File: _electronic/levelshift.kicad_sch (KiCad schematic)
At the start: 10 parts

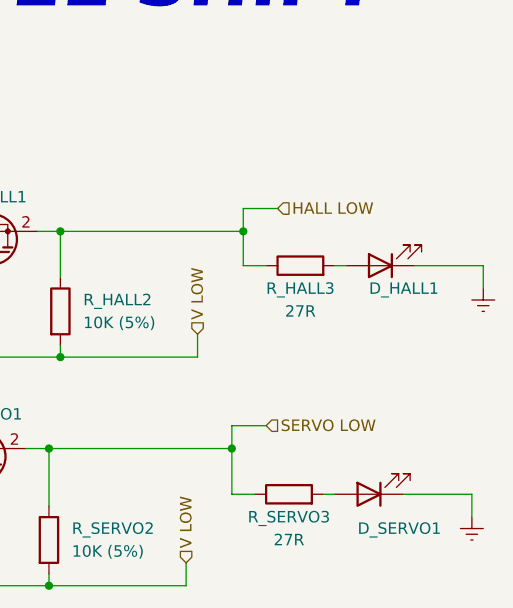
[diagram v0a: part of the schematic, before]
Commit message: revised pcb: direct power, leds, ftdi w/o 3v3
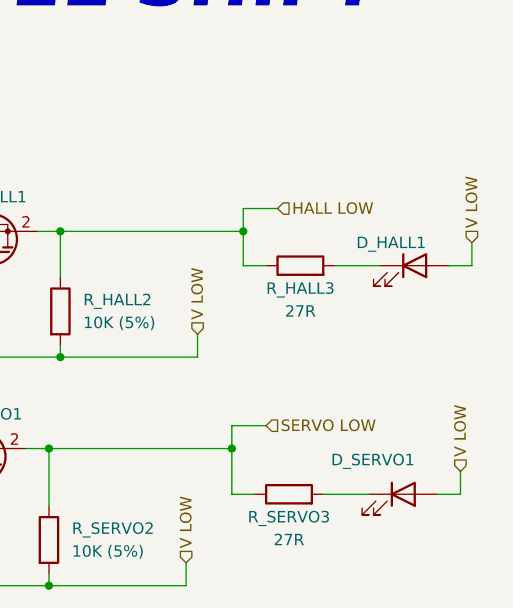
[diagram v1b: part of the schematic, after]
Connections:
- net V LOW: now also D_HALL1.2 (A), D_SERVO1.2 (A)
- net at R_HALL3.2: now also D_HALL1.1 (K); no longer D_HALL1.2 (A)
- net at R_SERVO3.2: now also D_SERVO1.1 (K); no longer D_SERVO1.2 (A)
- removed net GNDREF: D_HALL1.1 (K), D_SERVO1.1 (K)
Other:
- moved on the sheet: D_HALL1, D_SERVO1
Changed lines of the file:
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@@
     (stroke (width 0) (type default) (color 0 0 0 0))
   )
-  (wire (pts (xy 176.53 96.52) (xy 177.8 96.52))
+  (wire (pts (xy 176.53 96.52) (xy 181.61 96.52))
     (stroke (width 0) (type default) (color 0 0 0 0))
   )
@@
     (stroke (width 0) (type default) (color 0 0 0 0))
   )
+  (wire (pts (xy 191.77 93.98) (xy 191.77 96.52))
+    (stroke (width 0) (type default) (color 0 0 0 0))
+  )
   (wire (pts (xy 144.78 132.08) (xy 144.78 130.81))
     (stroke (width 0) (type default) (color 0 0 0 0))
@@
     (stroke (width 0) (type default) (color 0 0 0 0))
   )
-  (wire (pts (xy 176.53 121.92) (xy 175.26 121.92))
+  (wire (pts (xy 180.34 121.92) (xy 175.26 121.92))
     (stroke (width 0) (type default) (color 0 0 0 0))
   )
@@
     (stroke (width 0) (type default) (color 0 0 0 0))
   )
+  (wire (pts (xy 190.5 119.38) (xy 190.5 121.92))
+    (stroke (width 0) (type default) (color 0 0 0 0))
+  )
   (wire (pts (xy 160.02 129.54) (xy 160.02 132.08))
     (stroke (width 0) (type default) (color 0 0 0 0))
@@
     (stroke (width 0) (type default) (color 0 0 0 0))
   )
-  (wire (pts (xy 184.15 121.92) (xy 191.77 121.92))
+  (wire (pts (xy 187.96 121.92) (xy 190.5 121.92))
     (stroke (width 0) (type default) (color 0 0 0 0))
   )
@@
     (stroke (width 0) (type default) (color 0 0 0 0))
   )
-  (wire (pts (xy 191.77 121.92) (xy 191.77 124.46))
-    (stroke (width 0) (type default) (color 0 0 0 0))
-  )
   (wire (pts (xy 161.29 106.68) (xy 161.29 104.14))
     (stroke (width 0) (type default) (color 0 0 0 0))
   )
-  (wire (pts (xy 193.04 96.52) (xy 193.04 99.06))
-    (stroke (width 0) (type default) (color 0 0 0 0))
-  )
-  (wire (pts (xy 185.42 96.52) (xy 193.04 96.52))
+  (wire (pts (xy 189.23 96.52) (xy 191.77 96.52))
     (stroke (width 0) (type default) (color 0 0 0 0))
   )
@@
     (effects (font (size 1.27 1.27)) (justify left))
   )
+  (hierarchical_label "V LOW" (shape input) (at 191.77 93.98 90)
+    (effects (font (size 1.27 1.27)) (justify left))
+  )
   (hierarchical_label "SERVO HIGH" (shape input) (at 115.57 116.84 180)
     (effects (font (size 1.27 1.27)) (justify right))
+  )
+  (hierarchical_label "V LOW" (shape input) (at 190.5 119.38 90)
+    (effects (font (size 1.27 1.27)) (justify left))
   )
   (hierarchical_label "V HIGH" (shape input) (at 118.11 104.14 90)
@@
     (pin "2")
   )
-  (symbol (lib_id "Device:LED") (at 181.61 96.52 180) (unit 1)
-    (in_bom yes) (on_board yes)
-    (property "Reference" "D_HALL1" (id 0) (at 180.34 99.06 0)
+  (symbol (lib_id "Device:LED") (at 185.42 96.52 0) (unit 1)
+    (in_bom yes) (on_board yes)
+    (property "Reference" "D_HALL1" (id 0) (at 186.69 93.98 0)
       (effects (font (size 1.27 1.27)) (justify right))
     )
-    (property "Value" "LED white" (id 1) (at 184.15 91.44 0)
+    (property "Value" "LED white" (id 1) (at 182.88 101.6 0)
       (effects (font (size 1.27 1.27)) (justify left) hide)
     )
-    (property "Footprint" "LED_SMD:LED_0603_1608Metric_Pad1.05x0.95mm_HandSolder" (id 2) (at 181.61 96.52 0)
-      (effects (font (size 1.27 1.27)) hide)
-    )
-    (property "Datasheet" "https://br.mouser.com/datasheet/2/348/smld12-e-1874545.pdf" (id 3) (at 181.61 96.52 0)
-      (effects (font (size 1.27 1.27)) hide)
-    )
-    (property "#" "SMLD12WBN1W1" (id 4) (at 184.15 92.71 90)
+    (property "Footprint" "LED_SMD:LED_0603_1608Metric_Pad1.05x0.95mm_HandSolder" (id 2) (at 185.42 96.52 0)
+      (effects (font (size 1.27 1.27)) hide)
+    )
+    (property "Datasheet" "https://br.mouser.com/datasheet/2/348/smld12-e-1874545.pdf" (id 3) (at 185.42 96.52 0)
+      (effects (font (size 1.27 1.27)) hide)
+    )
+    (property "#" "SMLD12WBN1W1" (id 4) (at 182.88 100.33 90)
       (effects (font (size 1.27 1.27) italic) (justify right) hide)
     )
-    (property "Description" "Signal LED" (id 5) (at 181.61 96.52 0)
-      (effects (font (size 1.27 1.27)) hide)
-    )
-    (property "Group" "Hall" (id 6) (at 181.61 96.52 0)
-      (effects (font (size 1.27 1.27)) hide)
-    )
-    (property "Mouser" "OK" (id 7) (at 181.61 96.52 0)
+    (property "Description" "Signal LED" (id 5) (at 185.42 96.52 0)
+      (effects (font (size 1.27 1.27)) hide)
+    )
+    (property "Group" "Hall" (id 6) (at 185.42 96.52 0)
+      (effects (font (size 1.27 1.27)) hide)
+    )
+    (property "Mouser" "OK" (id 7) (at 185.42 96.52 0)
       (effects (font (size 1.27 1.27)) hide)
     )
@@
     (pin "2")
   )
-  (symbol (lib_id "power:GNDREF") (at 193.04 99.06 0) (unit 1)
-    (in_bom yes) (on_board yes) (fields_autoplaced)
-    (property "Reference" "#PWR0192" (id 0) (at 193.04 105.41 0)
-      (effects (font (size 1.27 1.27)) hide)
-    )
-    (property "Value" "GNDREF" (id 1) (at 193.04 104.14 0)
-      (effects (font (size 1.27 1.27)) hide)
-    )
-    (property "Footprint" "" (id 2) (at 193.04 99.06 0)
-      (effects (font (size 1.27 1.27)) hide)
-    )
-    (property "Datasheet" "" (id 3) (at 193.04 99.06 0)
-      (effects (font (size 1.27 1.27)) hide)
-    )
-    (pin "1")
-  )
   (symbol (lib_id "Transistor_FET:BSS138") (at 138.43 95.25 90) (unit 1)
     (in_bom yes) (on_board yes)
@@
     (pin "3")
   )
-  (symbol (lib_id "Device:LED") (at 180.34 121.92 180) (unit 1)
-    (in_bom yes) (on_board yes)
-    (property "Reference" "D_SERVO1" (id 0) (at 179.07 125.73 0)
+  (symbol (lib_id "Device:LED") (at 184.15 121.92 0) (unit 1)
+    (in_bom yes) (on_board yes)
+    (property "Reference" "D_SERVO1" (id 0) (at 185.42 118.11 0)
       (effects (font (size 1.27 1.27)) (justify right))
     )
-    (property "Value" "LED white" (id 1) (at 182.88 116.84 0)
+    (property "Value" "LED white" (id 1) (at 181.61 127 0)
       (effects (font (size 1.27 1.27)) (justify left) hide)
     )
-    (property "Footprint" "LED_SMD:LED_0603_1608Metric_Pad1.05x0.95mm_HandSolder" (id 2) (at 180.34 121.92 0)
-      (effects (font (size 1.27 1.27)) hide)
-    )
-    (property "Datasheet" "https://br.mouser.com/datasheet/2/348/smld12-e-1874545.pdf" (id 3) (at 180.34 121.92 0)
-      (effects (font (size 1.27 1.27)) hide)
-    )
-    (property "#" "SMLD12WBN1W1" (id 4) (at 182.88 119.38 90)
+    (property "Footprint" "LED_SMD:LED_0603_1608Metric_Pad1.05x0.95mm_HandSolder" (id 2) (at 184.15 121.92 0)
+      (effects (font (size 1.27 1.27)) hide)
+    )
+    (property "Datasheet" "https://br.mouser.com/datasheet/2/348/smld12-e-1874545.pdf" (id 3) (at 184.15 121.92 0)
+      (effects (font (size 1.27 1.27)) hide)
+    )
+    (property "#" "SMLD12WBN1W1" (id 4) (at 181.61 124.46 90)
       (effects (font (size 1.27 1.27) italic) (justify right) hide)
     )
-    (property "Description" "Signal LED" (id 5) (at 180.34 121.92 0)
-      (effects (font (size 1.27 1.27)) hide)
-    )
-    (property "Group" "Servo" (id 6) (at 180.34 121.92 0)
-      (effects (font (size 1.27 1.27)) hide)
-    )
-    (property "Mouser" "OK" (id 7) (at 180.34 121.92 0)
+    (property "Description" "Signal LED" (id 5) (at 184.15 121.92 0)
+      (effects (font (size 1.27 1.27)) hide)
+    )
+    (property "Group" "Servo" (id 6) (at 184.15 121.92 0)
+      (effects (font (size 1.27 1.27)) hide)
+    )
+    (property "Mouser" "OK" (id 7) (at 184.15 121.92 0)
       (effects (font (size 1.27 1.27)) hide)
     )
@@
     (pin "2")
   )
-  (symbol (lib_id "power:GNDREF") (at 191.77 124.46 0) (unit 1)
-    (in_bom yes) (on_board yes) (fields_autoplaced)
-    (property "Reference" "#PWR0191" (id 0) (at 191.77 130.81 0)
-      (effects (font (size 1.27 1.27)) hide)
-    )
-    (property "Value" "GNDREF" (id 1) (at 191.77 129.54 0)
-      (effects (font (size 1.27 1.27)) hide)
-    )
-    (property "Footprint" "" (id 2) (at 191.77 124.46 0)
-      (effects (font (size 1.27 1.27)) hide)
-    )
-    (property "Datasheet" "" (id 3) (at 191.77 124.46 0)
-      (effects (font (size 1.27 1.27)) hide)
-    )
-    (pin "1")
-  )
   (symbol (lib_id "Transistor_FET:BSS138") (at 137.16 119.38 90) (unit 1)

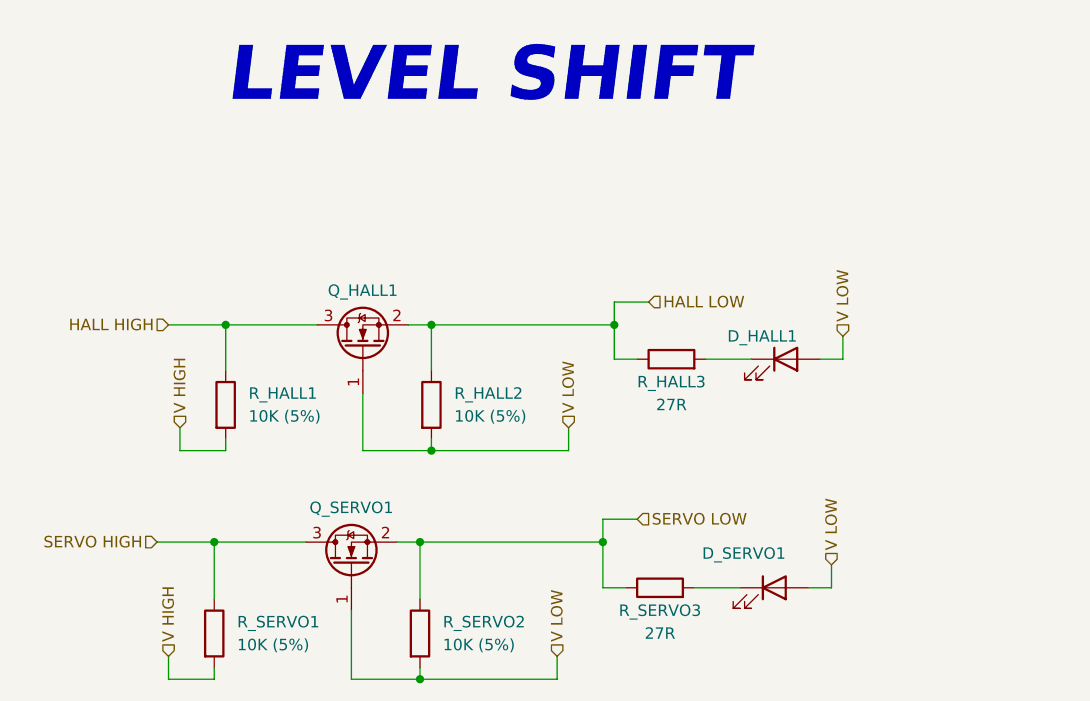
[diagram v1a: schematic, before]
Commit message: led resistor revision, b.o.m. and pcb anotation
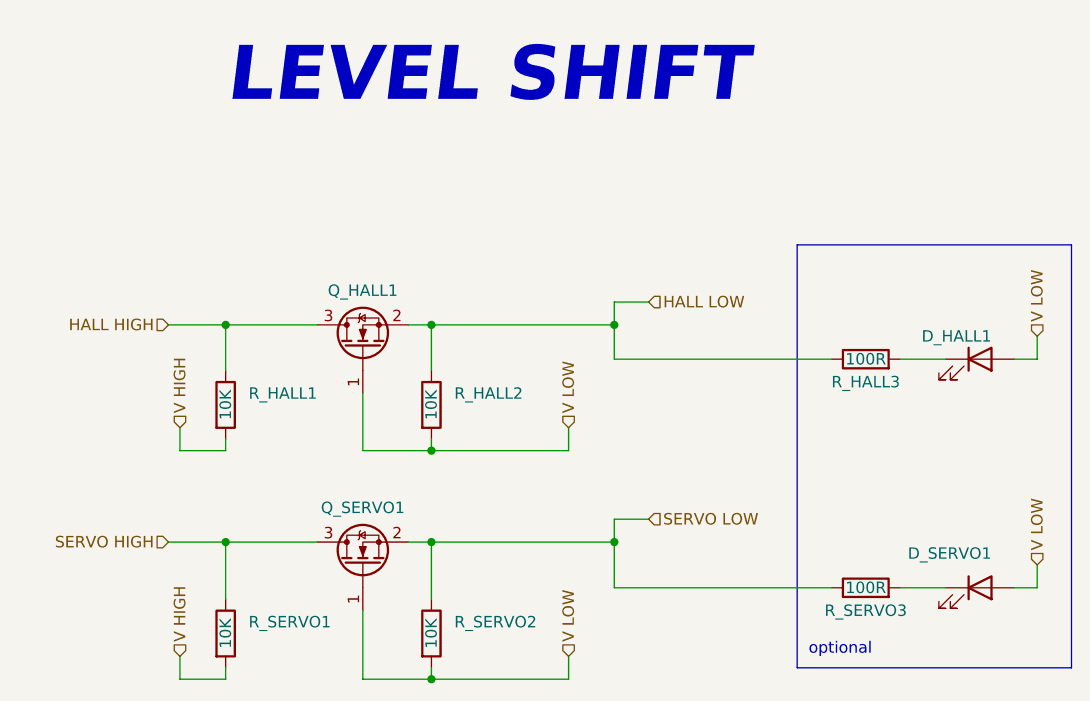
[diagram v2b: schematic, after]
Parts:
- R_HALL1, R_HALL2, R_SERVO1, R_SERVO2: value 10K (5%) -> 10K; # CHP0603AFX-1002ELF -> ERJ-3EKF1002V
- R_HALL3, R_SERVO3: value 27R -> 100R; # CMP0603-FX-27R0ELF -> ERJ-3EKF1000V
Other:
- note added: "optional"
- moved on the sheet: D_HALL1, D_SERVO1, Q_SERVO1, R_HALL3, R_SERVO1, R_SERVO2, R_SERVO3

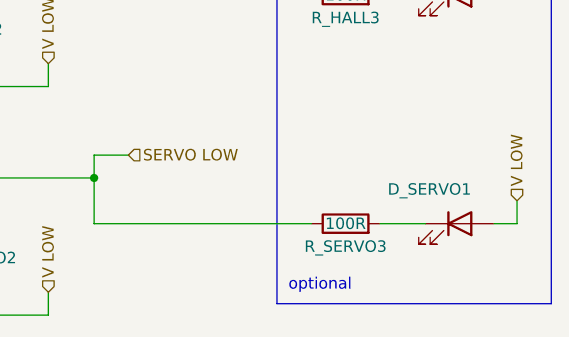
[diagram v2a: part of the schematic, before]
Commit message: schematics and pcb cleanup
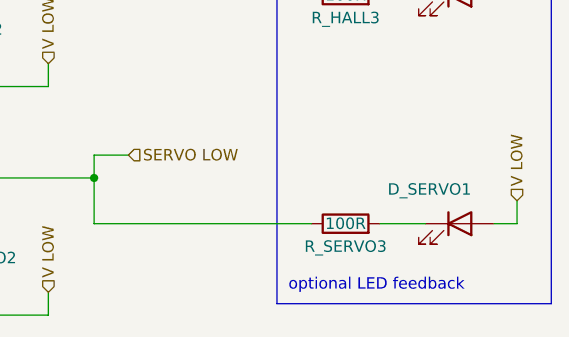
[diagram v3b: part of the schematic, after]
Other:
- note added: "optional LED feedback"
- note removed: "optional"
- title: E-TKT -> E-TKT v1.0
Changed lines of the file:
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@@
   (paper "A4")
   (title_block
-    (title "E-TKT")
-    (date "2022-07-21")
-    (rev "3")
+    (title "E-TKT v1.0")
+    (date "2022-09-29")
+    (rev "4")
     (company "Andrei Speridiao")
   )
@@
     (stroke (width 0) (type default) (color 0 0 0 0))
   )
-  (text "optional" (at 187.96 129.54 0)
+  (text "optional LED feedback" (at 187.96 129.54 0)
     (effects (font (size 1.27 1.27)) (justify left bottom))
   )
